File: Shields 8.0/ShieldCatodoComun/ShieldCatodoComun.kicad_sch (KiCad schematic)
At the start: 4 parts, among them J1 Power, J2 Digital/PWM, J3 Analog, J4 Digital/PWM

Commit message: Añadiendo proyecto kicad8.0 Catodo Común
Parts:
- added Q1, Q2, Q3: 2N2219, Package_TO_SOT_THT:TO-39-3, symbol Transistor_BJT:2N2219
- added R1, R10, R11, R2, R3, R4, R5, R6, R7, R8, R9: R, symbol Device:R
- added RV2: R_Potentiometer, symbol Device:R_Potentiometer
- added U1, U2, U3: D168K, Display_7Segment:D1X8K, symbol Display_Character:D168K
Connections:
- net *10: now also R11.1
- net *3: now also R5.1
- net *5: now also R3.1
- net *6: now also R2.1
- net *9: now also R10.1
- net +5V: now also RV2.1
- net 2: now also R6.1
- net 4: now also R4.1
- net 7: now also R1.1
- net 8: now also R9.1
- net A0: now also RV2.2
- net GND: now also Q1.1 (E), Q2.1 (E), Q3.1 (E), RV2.3
- net RX/0: now also R8.1
- net TX/1: now also R7.1
- new net: R4.2, U1.1 (E), U2.1 (E), U3.1 (E)
- new net: Q1.2 (B), R9.2
- new net: R3.2, U1.9 (F), U2.9 (F), U3.9 (F)
- new net: Q2.2 (B), R10.2
- new net: R2.2, U1.10 (G), U2.10 (G), U3.10 (G)
- new net: R5.2, U1.2 (D), U2.2 (D), U3.2 (D)
- new net: Q1.3 (C), U1.3 (CC), U1.8 (CC)
- new net: R6.2, U1.4 (C), U2.4 (C), U3.4 (C)
- new net: R1.2, U1.5 (DP), U2.5 (DP), U3.5 (DP)
- new net: R7.2, U1.6 (B), U2.6 (B), U3.6 (B)
- new net: R8.2, U1.7 (A), U2.7 (A), U3.7 (A)
- new net: Q2.3 (C), U2.3 (CC), U2.8 (CC)
- new net: Q3.2 (B), R11.2
- new net: Q3.3 (C), U3.3 (CC), U3.8 (CC)

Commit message: Implementacion del PCB
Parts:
- R1, R10, R11, R2, R3, R4, R5, R6, R7, R8, R9: footprint (none) -> Resistor_THT:R_Axial_DIN0207_L6.3mm_D2.5mm_P10.16mm_Horizontal
- RV2: footprint (none) -> Potentiometer_THT:Potentiometer_Alpha_RD901F-40-00D_Single_Vertical
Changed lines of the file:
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@@
 			)
 		)
-		(property "Footprint" ""
+		(property "Footprint" "Resistor_THT:R_Axial_DIN0207_L6.3mm_D2.5mm_P10.16mm_Horizontal"
 			(at 128.27 89.408 90)
 			(effects
@@
 			)
 		)
-		(property "Footprint" ""
+		(property "Footprint" "Resistor_THT:R_Axial_DIN0207_L6.3mm_D2.5mm_P10.16mm_Horizontal"
 			(at 163.83 114.808 90)
 			(effects
@@
 			)
 		)
-		(property "Footprint" ""
+		(property "Footprint" "Resistor_THT:R_Axial_DIN0207_L6.3mm_D2.5mm_P10.16mm_Horizontal"
 			(at 133.35 91.948 90)
 			(effects
@@
 			)
 		)
-		(property "Footprint" ""
+		(property "Footprint" "Resistor_THT:R_Axial_DIN0207_L6.3mm_D2.5mm_P10.16mm_Horizontal"
 			(at 195.58 114.808 90)
 			(effects
@@
 			)
 		)
-		(property "Footprint" ""
+		(property "Footprint" "Resistor_THT:R_Axial_DIN0207_L6.3mm_D2.5mm_P10.16mm_Horizontal"
 			(at 113.03 81.788 90)
 			(effects
@@
 			)
 		)
-		(property "Footprint" ""
+		(property "Footprint" "Resistor_THT:R_Axial_DIN0207_L6.3mm_D2.5mm_P10.16mm_Horizontal"
 			(at 107.95 79.248 90)
 			(effects
@@
 			)
 		)
-		(property "Footprint" ""
+		(property "Footprint" "Resistor_THT:R_Axial_DIN0207_L6.3mm_D2.5mm_P10.16mm_Horizontal"
 			(at 118.11 84.328 90)
 			(effects
@@
 			)
 		)
-		(property "Footprint" ""
+		(property "Footprint" "Resistor_THT:R_Axial_DIN0207_L6.3mm_D2.5mm_P10.16mm_Horizontal"
 			(at 232.41 114.808 90)
 			(effects
@@
 			)
 		)
-		(property "Footprint" ""
+		(property "Footprint" "Resistor_THT:R_Axial_DIN0207_L6.3mm_D2.5mm_P10.16mm_Horizontal"
 			(at 143.51 97.028 90)
 			(effects
@@
 			)
 		)
-		(property "Footprint" ""
+		(property "Footprint" "Resistor_THT:R_Axial_DIN0207_L6.3mm_D2.5mm_P10.16mm_Horizontal"
 			(at 123.19 86.868 90)
 			(effects
@@
 			)
 		)
-		(property "Footprint" ""
+		(property "Footprint" "Potentiometer_THT:Potentiometer_Alpha_RD901F-40-00D_Single_Vertical"
 			(at 29.21 90.17 0)
 			(effects
@@
 			)
 		)
-		(property "Footprint" ""
+		(property "Footprint" "Resistor_THT:R_Axial_DIN0207_L6.3mm_D2.5mm_P10.16mm_Horizontal"
 			(at 138.43 94.488 90)
 			(effects

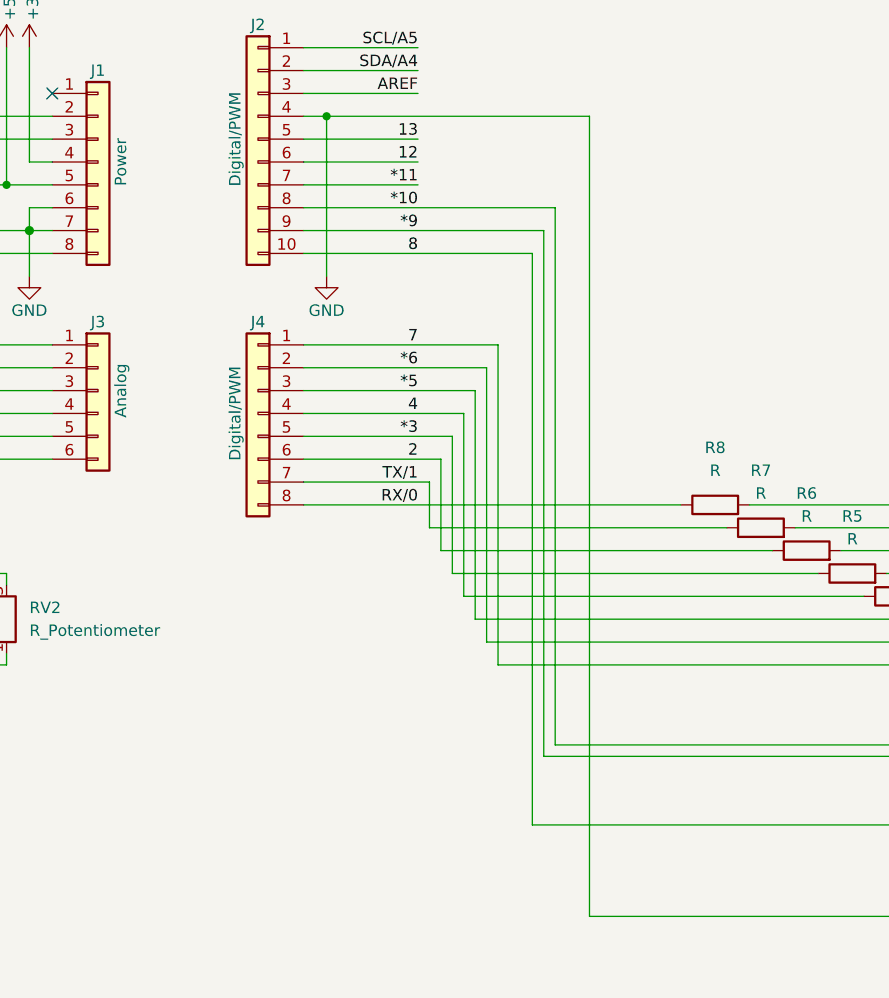
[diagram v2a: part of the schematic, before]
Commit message: Agregado de jumpers
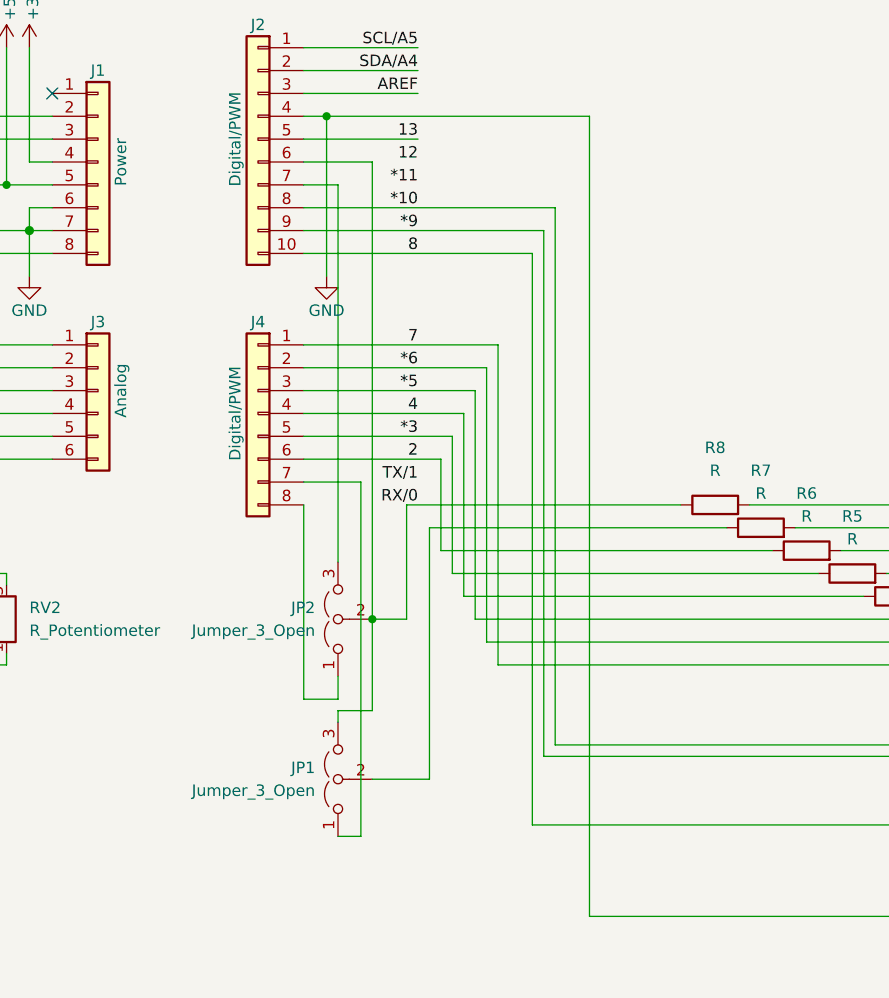
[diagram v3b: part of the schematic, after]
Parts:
- added JP1, JP2: Jumper_3_Open, symbol Jumper:Jumper_3_Open
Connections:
- net *11: no longer J2.7 (Pin_7)
- net 12: no longer J2.6 (Pin_6)
- net RX/0: now also J2.6 (Pin_6), JP1.3 (B), JP2.2 (C); no longer J4.8 (Pin_8)
- net TX/1: no longer J4.7 (Pin_7), R7.1
- new net: J2.7 (Pin_7), JP2.3 (B)
- new net: J4.7 (Pin_7), JP1.1 (A)
- new net: J4.8 (Pin_8), JP2.1 (A)
- new net: JP1.2 (C), R7.1
